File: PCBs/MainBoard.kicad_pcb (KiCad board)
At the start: 2 copper layers, 40.4 x 70 mm, 52 parts, among them J1 USB_C_Receptacle, J2 Conn_01x12_FPC_0.5mm, J3 Conn_01x08, J4 Qwiic_RA, J5 SM06B-GHS-TB, SW1 PTH_RA_h7.5mm, SW2 SMD_4.6x2.8mm_h2.5mm, SW3 SMD_4.6x2.8mm_h2.5mm, U1 TVS_ESD_USB, U2 ESP32-S3-MINI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

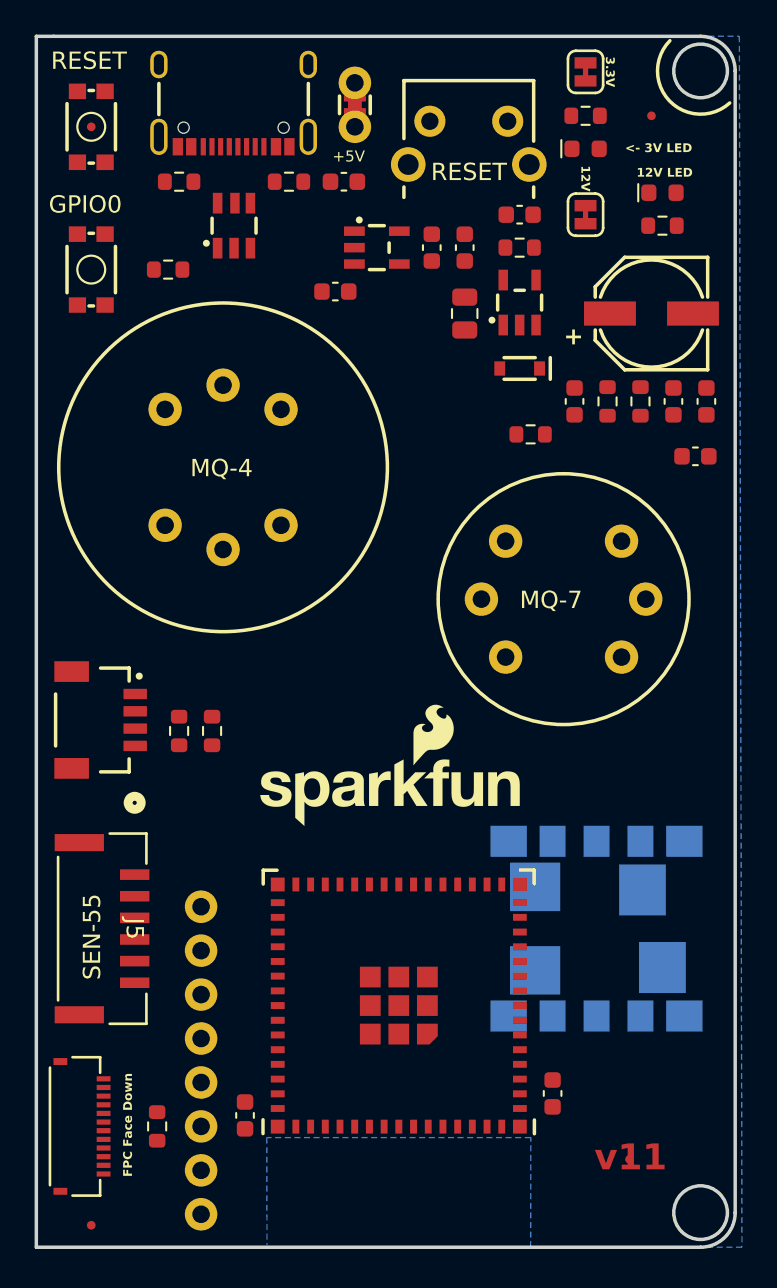
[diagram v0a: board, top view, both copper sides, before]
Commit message: Routing Main Board
Updated from google drive comments and routed main board PCB
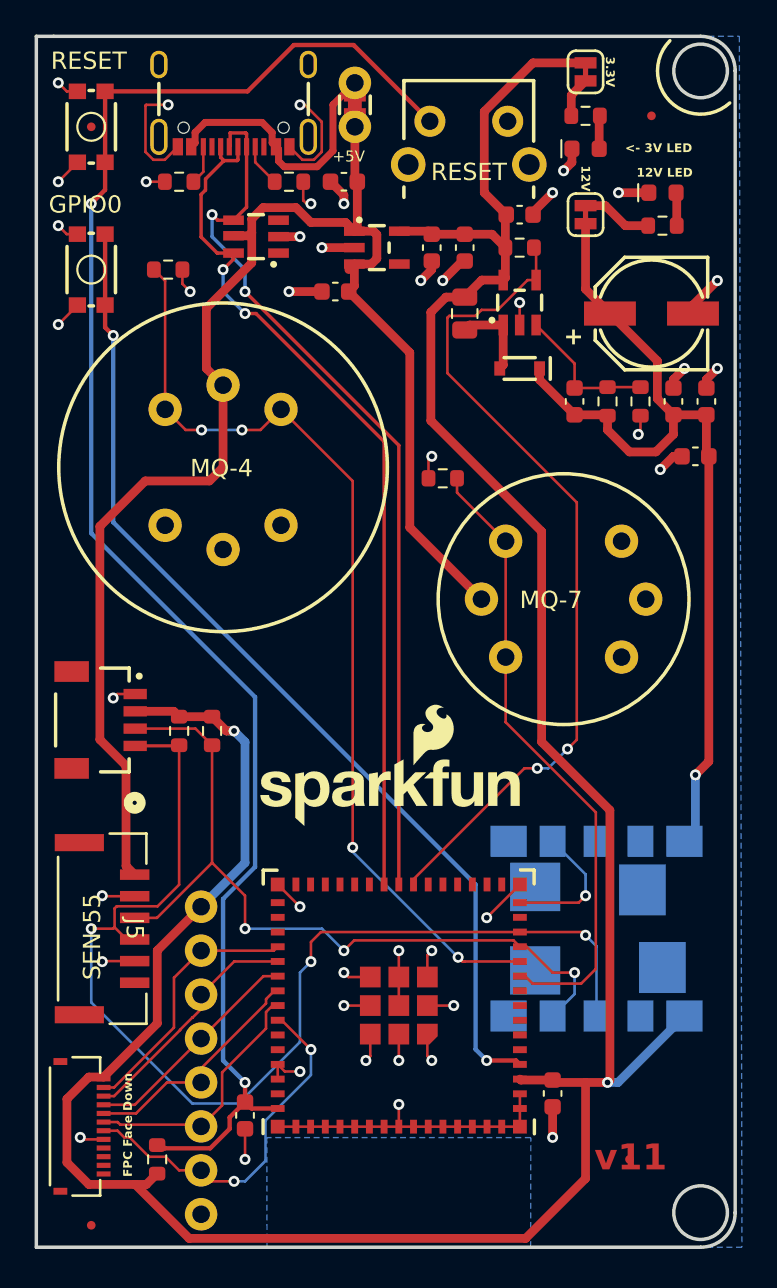
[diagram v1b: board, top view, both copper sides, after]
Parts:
- moved R11 5.68 mm to (152.3, 79.5)
- moved R10 1.91 mm to (139.0, 94.1)
- moved R8 1.91 mm to (137.1, 94.1)
- moved R3 1.90 mm to (135.8, 118.8), turned to 90 degrees
- moved U1 1.42 mm to (141.5, 65.5), turned to 180 degrees
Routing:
- net +3.3V: track 0.00 -> 165.8 mm, vias 0 -> 2
- net GND: track 0.00 -> 95.8 mm, vias 0 -> 43
- net RESET: track 0.00 -> 94.4 mm, vias 0 -> 2
- net +5V: track 0.00 -> 86.7 mm
- net SCL: track 0.00 -> 68.7 mm, vias 0 -> 3
- net ESP0: track 0.00 -> 58.9 mm, vias 0 -> 2
- net ESP11/MQ4: track 0.00 -> 55.7 mm, vias 0 -> 4
- net +12V: track 0.00 -> 52.5 mm, vias 0 -> 1
- net D-: track 0.00 -> 51.7 mm, vias 0 -> 2
- net D+: track 0.00 -> 50.7 mm, vias 0 -> 2
- net ~{SHDN}-EN: track 0.00 -> 48.5 mm, vias 0 -> 2
- net SDA: track 0.00 -> 45.7 mm, vias 0 -> 3
- net ESP10/MQ7: track 0.00 -> 36.6 mm
- net ~{RST}: track 0.00 -> 21.2 mm, vias 0 -> 2
- net Net-(JP1-A): track 0.00 -> 15.8 mm
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
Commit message: Updates
Fixing connections between epaper display board and main board pcbs
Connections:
- J2 pad 3: SCLK -> ~{RST}
- J2 pad 4: SDIO -> D/~{C}
- J2 pad 6: D/~{C} -> SCLK
- J2 pad 7: ~{RST} -> SDIO
- J3 pad 3: SCLK -> ~{RST}
- J3 pad 4: SDIO -> D/~{C}
- J3 pad 6: D/~{C} -> SCLK
- J3 pad 7: ~{RST} -> SDIO
- U2 pad 35: SCLK -> ~{RST}
- U2 pad 36: SDIO -> D/~{C}
- U2 pad 38: D/~{C} -> SCLK
- U2 pad 39: ~{RST} -> SDIO
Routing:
- net SDIO: track 13.1 -> 21.2 mm, vias 0 -> 2
- net ~{RST}: track 21.2 -> 13.8 mm, vias 2 -> 0
- net D/~{C}: track 14.7 -> 13.1 mm
- net SCLK: track 13.8 -> 14.7 mm

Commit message: Main PCB update
Updated per comments in google doc
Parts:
- removed J5: SM06B-GHS-TB, SM06B-GHS-TB:CONN_SM06B-GHS-TB_JST
- removed the Ref** at (132.0, 59.1)
- removed the Ref** at (163.1, 118.8)
- removed the Ref** at (164.4, 58.5)
- removed the Ref** at (132.0, 122.6)
- added FID1: Fiducial_0.5mm, SparkFun-Aesthetic:Fiducial_0.5mm_Mask1mm, F.Cu at (164.4, 120.7)
- added FID2: Fiducial_0.5mm, SparkFun-Aesthetic:Fiducial_0.5mm_Mask1mm, F.Cu at (132.0, 59.1)
- added FID3: Fiducial_0.5mm, SparkFun-Aesthetic:Fiducial_0.5mm_Mask1mm, F.Cu at (164.4, 58.5)
- added FID4: Fiducial_0.5mm, SparkFun-Aesthetic:Fiducial_0.5mm_Mask1mm, F.Cu at (131.3, 122.6)
- added Ref**: Val**, SparkFun-Aesthetic:OSHW_Logo_6mm, B.Cu at (164.9, 117.5)
- added ST1: Stand_off, SparkFun-Hardware:STAND-OFF, F.Cu at (167.2, 55.9)
- added U8: SEN54, SparkFun-Connector:JST-6-SMD-1.25MM-LOCKING, F.Cu at (131.3, 105.5)
- added kibuzzard-65B1D3B2: G***, kibuzzard-65B1D3B2, F.Cu at (159.5, 70.4)
- added kibuzzard-65B1D56F: G***, kibuzzard-65B1D56F, F.Cu at (132.0, 55.4)
- added kibuzzard-65B1D57E: G***, kibuzzard-65B1D57E, F.Cu at (132.0, 63.6)
- added kibuzzard-65B1D5D4: G***, kibuzzard-65B1D5D4, F.Cu at (141.9, 78.7)
- added kibuzzard-65B1D5EA: G***, kibuzzard-65B1D5EA, F.Cu at (159.2, 86.3)
- added kibuzzard-65B1D64A: G***, kibuzzard-65B1D64A, F.Cu at (153.8, 61.7)
- added kibuzzard-65B1D673: G***, kibuzzard-65B1D673, B.Cu at (147.2, 61.0)
- added kibuzzard-65B1DFAF: G***, kibuzzard-65B1DFAF, B.Cu at (167.8, 105.1)
- added kibuzzard-65B1E0D1: G***, kibuzzard-65B1E0D1, F.Cu at (129.6, 105.4)
- added kibuzzard-65B1E10A: G***, kibuzzard-65B1E10A, B.Cu at (135.4, 104.1)
- added kibuzzard-65B1E11D: G***, kibuzzard-65B1E11D, B.Cu at (135.4, 106.8)
- added kibuzzard-65B1E12C: G***, kibuzzard-65B1E12C, B.Cu at (135.7, 109.4)
- added kibuzzard-65B1E13C: G***, kibuzzard-65B1E13C, B.Cu at (136.0, 111.8)
- added kibuzzard-65B1E14E: G***, kibuzzard-65B1E14E, B.Cu at (135.2, 114.5)
- added kibuzzard-65B1E160: G***, kibuzzard-65B1E160, B.Cu at (135.5, 116.8)
- added kibuzzard-65B1E16C: G***, kibuzzard-65B1E16C, B.Cu at (135.5, 119.3)
- added kibuzzard-65B1E179: G***, kibuzzard-65B1E179, B.Cu at (135.3, 122.0)
- added kibuzzard-65B1E2D2: G***, kibuzzard-65B1E2D2, F.Cu at (165.0, 61.7)
- added kibuzzard-65B1E2FB: G***, kibuzzard-65B1E2FB, F.Cu at (164.4, 60.4)
- added kibuzzard-65B1E40B: G***, kibuzzard-65B1E40B, F.Cu at (130.3, 116.9)
- added kibuzzard-65B1E438: G***, kibuzzard-65B1E438, B.Cu at (148.9, 82.5)
- moved C9 18.6 mm to (164.4, 96.6)
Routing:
- net GND: track 95.8 -> 97.6 mm
- net +12V: track 52.5 -> 54.3 mm
- net Net-(JP1-A): track 15.8 -> 14.8 mm
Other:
- board text added: "v11.2"
- board text removed: "+"
- board text removed: "+5V"
- board text removed: "12V LED"
- board text removed: "<- 3V LED"
- board text removed: "FPC Face Down"
- board text removed: "GPIO0"
- board text removed: "MQ-4"
- board text removed: "MQ-7"
- board text removed: "RESET"
- board text removed: "SEN-55"
- board text removed: "SparkFun Home Air Quality Monitor Main Enclosure PCB V11 Capstone F23 - The Band Author: Anton Vandenberge"
- board text removed: "v11"

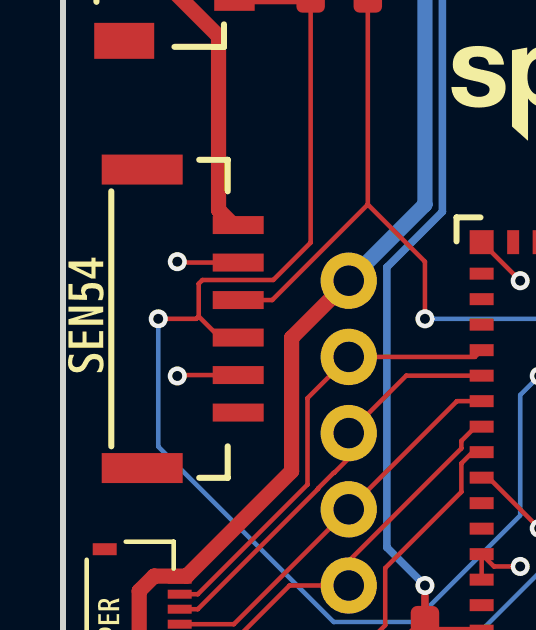
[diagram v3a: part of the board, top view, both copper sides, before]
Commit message: Updated SEN55
Brought back the SEN55 to the board
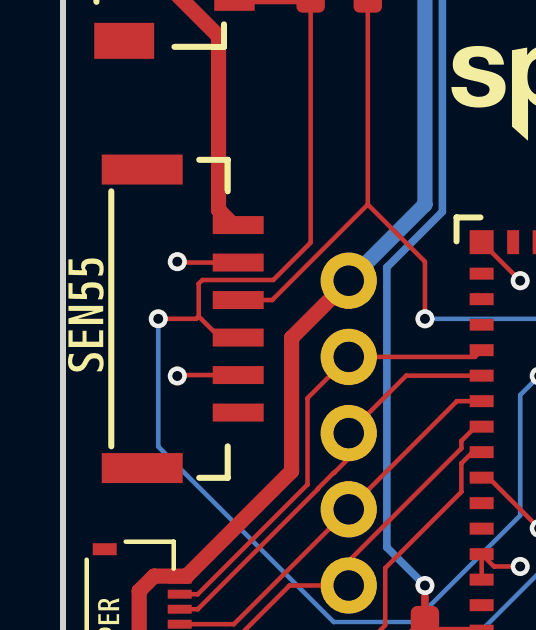
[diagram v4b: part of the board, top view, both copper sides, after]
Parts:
- removed kibuzzard-65B1E0D1: G***, kibuzzard-65B1E0D1
- added kibuzzard-65B27CA0: G***, kibuzzard-65B27CA0, F.Cu at (129.6, 105.4)
- U8: value SEN54 -> SEN55
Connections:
- C7 pad +: +12V -> (no net)
- C7 pad -: GND -> (no net)
